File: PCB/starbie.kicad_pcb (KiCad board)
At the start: 2 copper layers, 125.5 x 85.8 mm, 11 parts, among them J1 Conn_01x04_Pin, J2 Conn_01x08_Pin, SW1 SW_Push, SW2 SW_Push, U1 XIAO-ESP32-C3-SMD, U2 DHT11

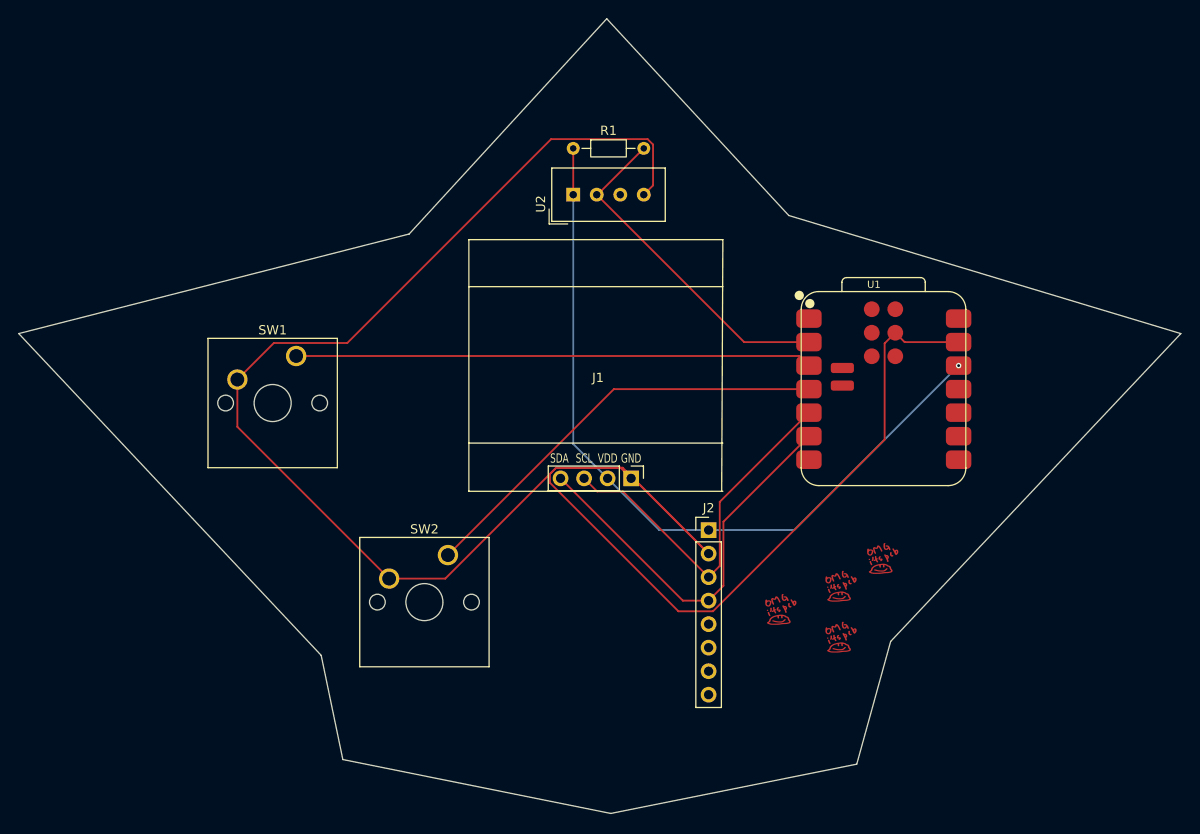
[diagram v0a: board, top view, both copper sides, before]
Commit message: added buzzer to pcb
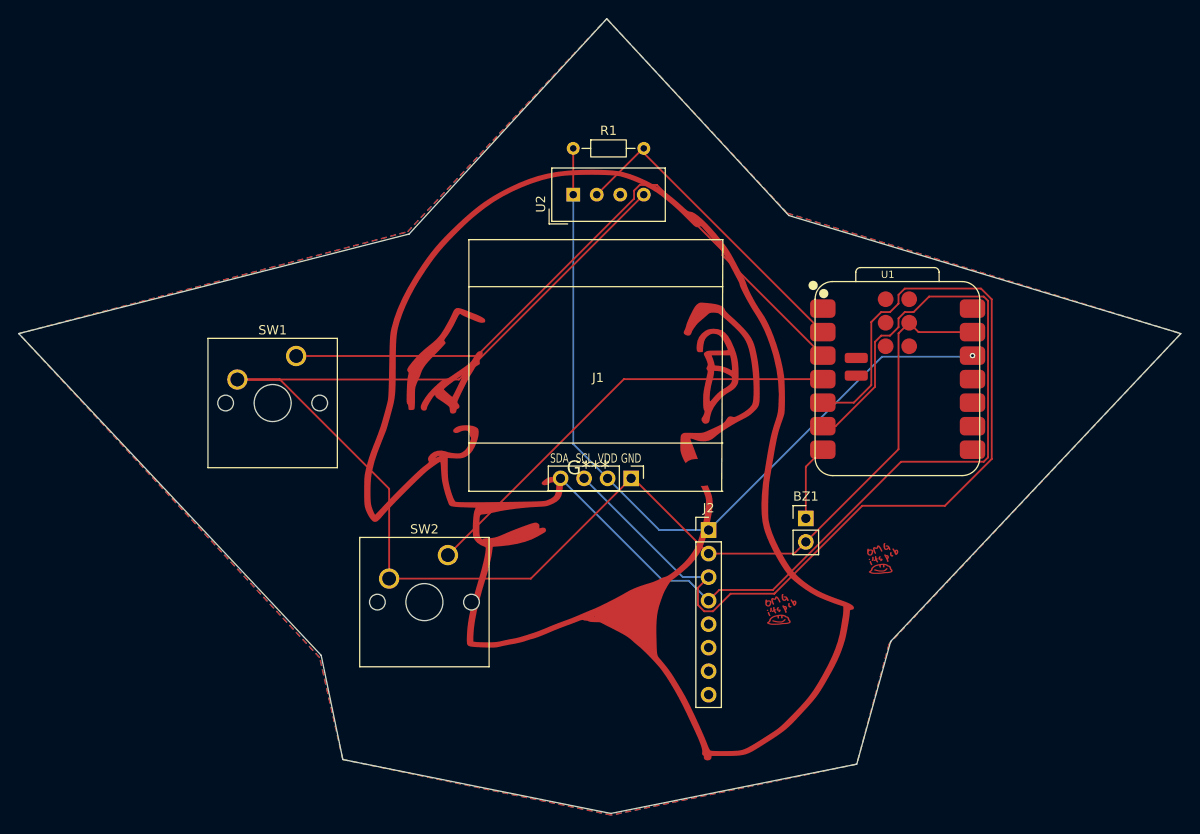
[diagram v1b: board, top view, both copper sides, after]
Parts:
- removed the G*** at (174.0, 109.0)
- removed the G*** at (174.0, 103.5)
- added BZ1: Buzzer, Connector_PinHeader_2.54mm:PinHeader_1x02_P2.54mm_Vertical, F.Cu at (170.5, 96.0)
- added G***: LOGO, LOGO, F.Cu at (147.0, 90.5)
- moved U1 1.85 mm to (171.5, 91.4)
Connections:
- U1 pad 7: unconnected-(U1-D6-Pad7) -> /BUZZER
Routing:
- net /SCL: track 40.1 -> 105.8 mm
- net /SDA: track 43.7 -> 102.2 mm
- net GND: track 224.8 -> 172.1 mm
- net /GPIO2: track 55.8 -> 73.0 mm
- net /BUZZER: track 0.00 -> 8.18 mm
- net +3.3V: track 84.7 -> 86.8 mm
- net /GPIO3: track 46.4 -> 48.4 mm
- net /DHT11 DATA: track 36.7 -> 35.0 mm
- added copper zone on B.Cu, net GND
- added copper zone on F.Cu, net GND

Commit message: put image on silkscreen not copper
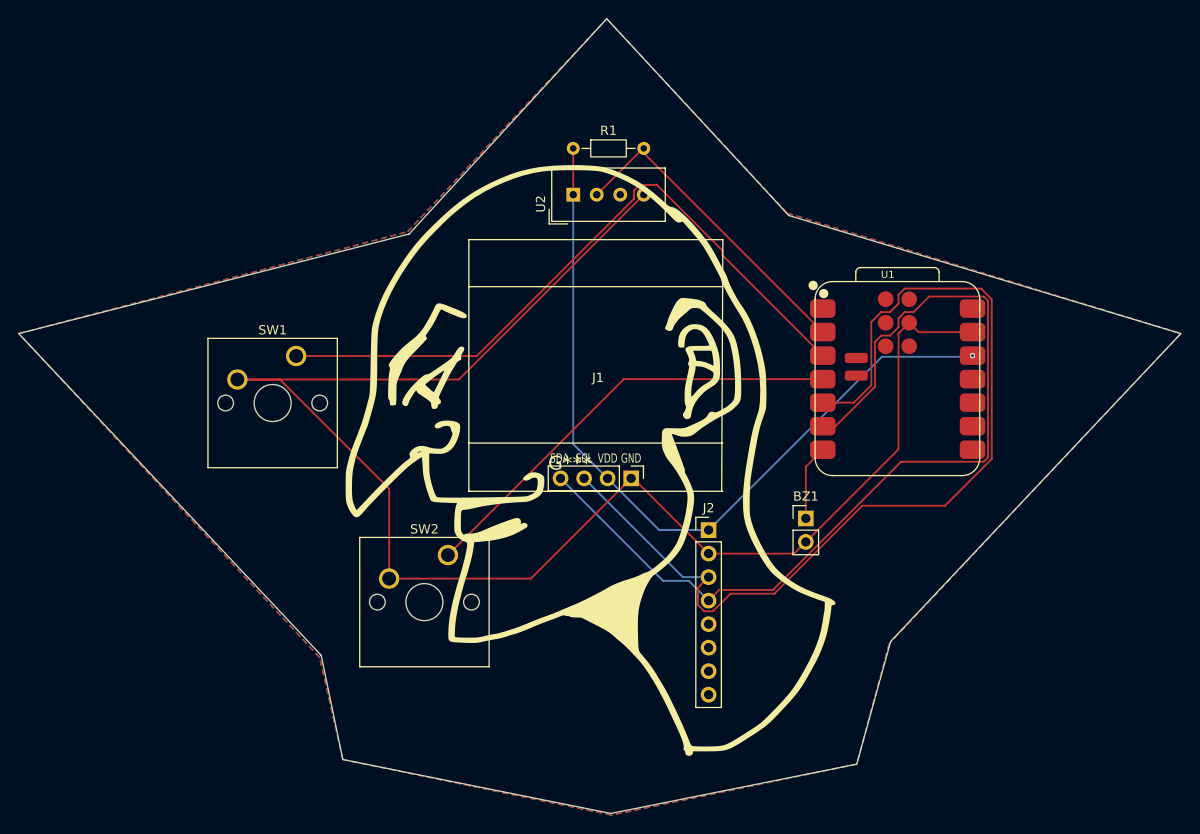
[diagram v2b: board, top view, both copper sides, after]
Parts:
- removed the G*** at (178.5, 100.5)
- removed the G*** at (167.5, 106.0)
- moved G*** 2.06 mm to (145.0, 90.0)

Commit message: realized wrong buzzer, changed pcb routing again
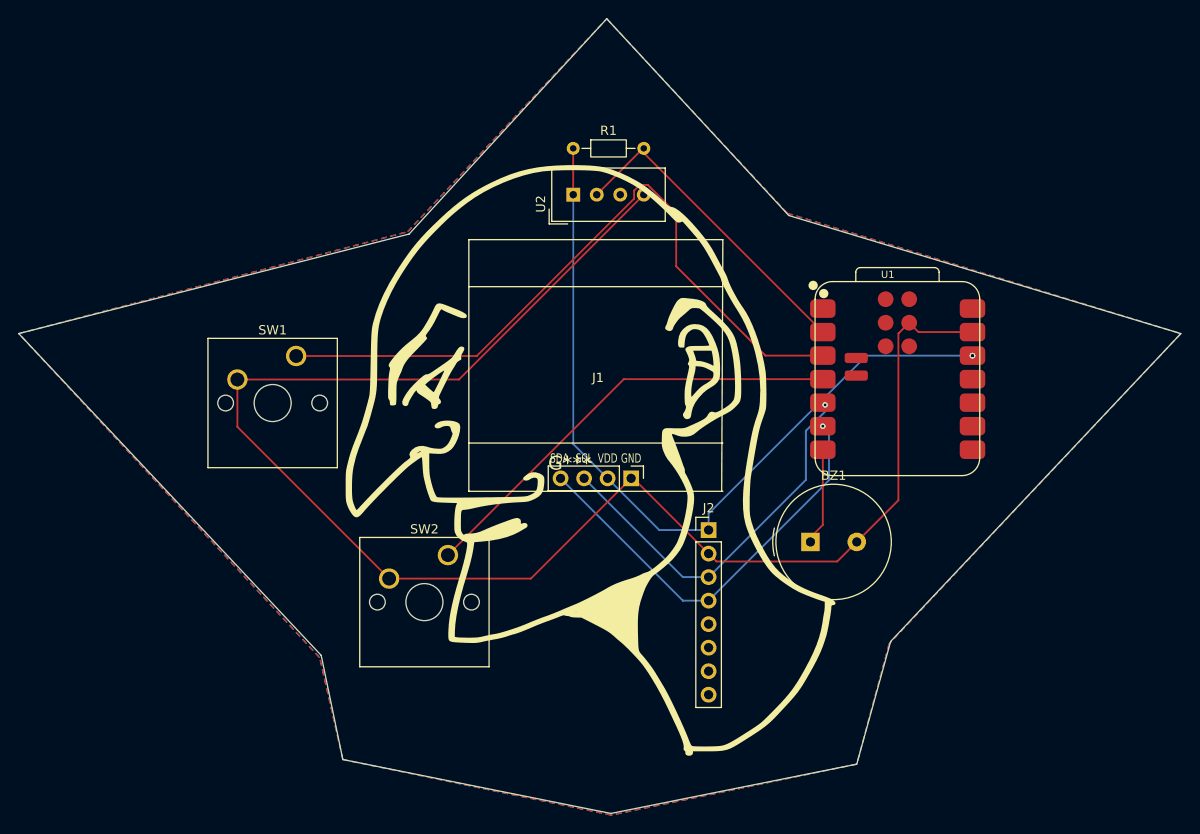
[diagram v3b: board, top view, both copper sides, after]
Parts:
- BZ1: footprint Connector_PinHeader_2.54mm:PinHeader_1x02_P2.54mm_Vertical -> Buzzer_Beeper:Buzzer_TDK_PS1240P02BT_D12.2mm_H6.5mm
- moved BZ1 2.59 mm to (171.0, 98.5)
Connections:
- BZ1 pad 2: GND -> unconnected-(BZ1---Pad2)
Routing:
- net /SCL: track 105.8 -> 41.7 mm, vias 0 -> 1
- net /SDA: track 102.2 -> 46.0 mm, vias 0 -> 1
- net /GPIO2: track 73.0 -> 76.0 mm
- net /BUZZER: track 8.18 -> 10.5 mm
- net GND: track 172.1 -> 173.3 mm
- net +3.3V: track 86.8 -> 87.7 mm, vias 1 -> 2
